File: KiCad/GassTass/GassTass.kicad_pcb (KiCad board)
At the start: 2 copper layers, 3 parts, among them U1 Arduino_Nano_v3.x, U2 ATmega328P-PU

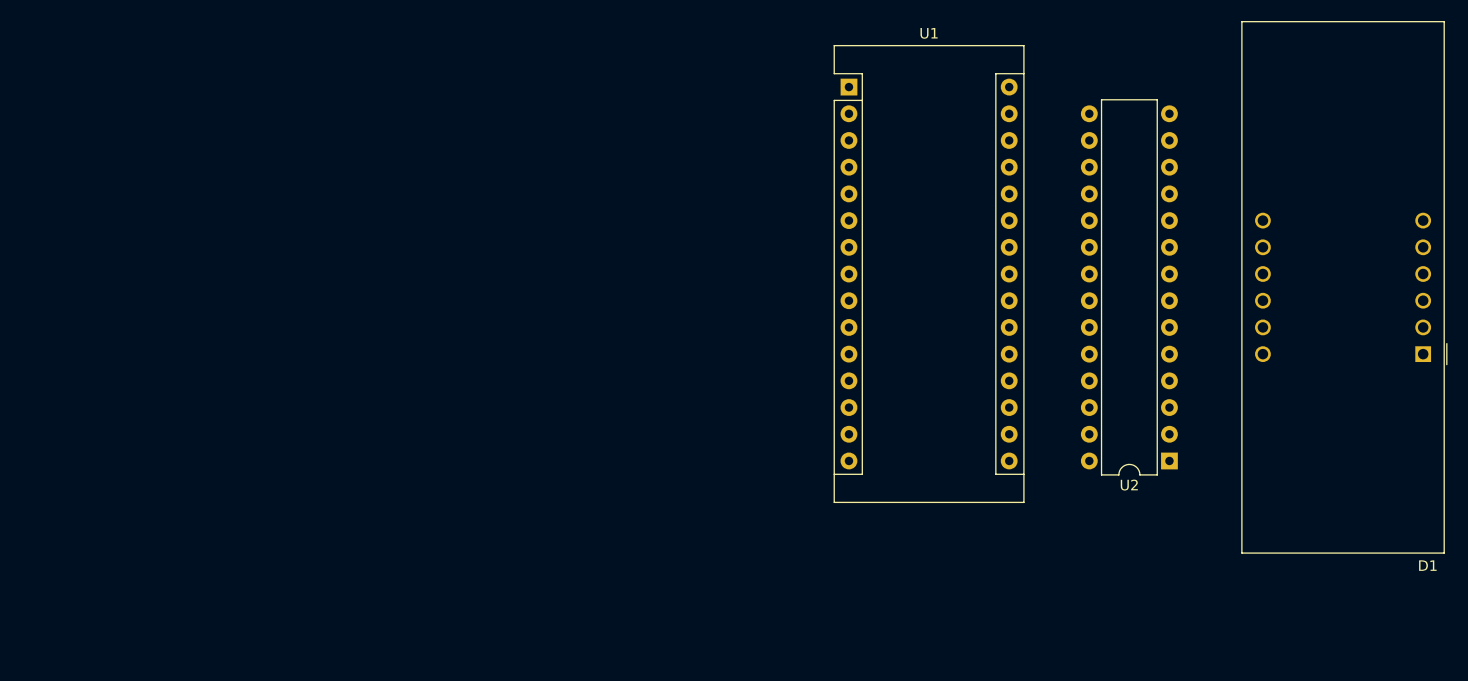
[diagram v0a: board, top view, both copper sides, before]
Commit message: at it again, adding transistors
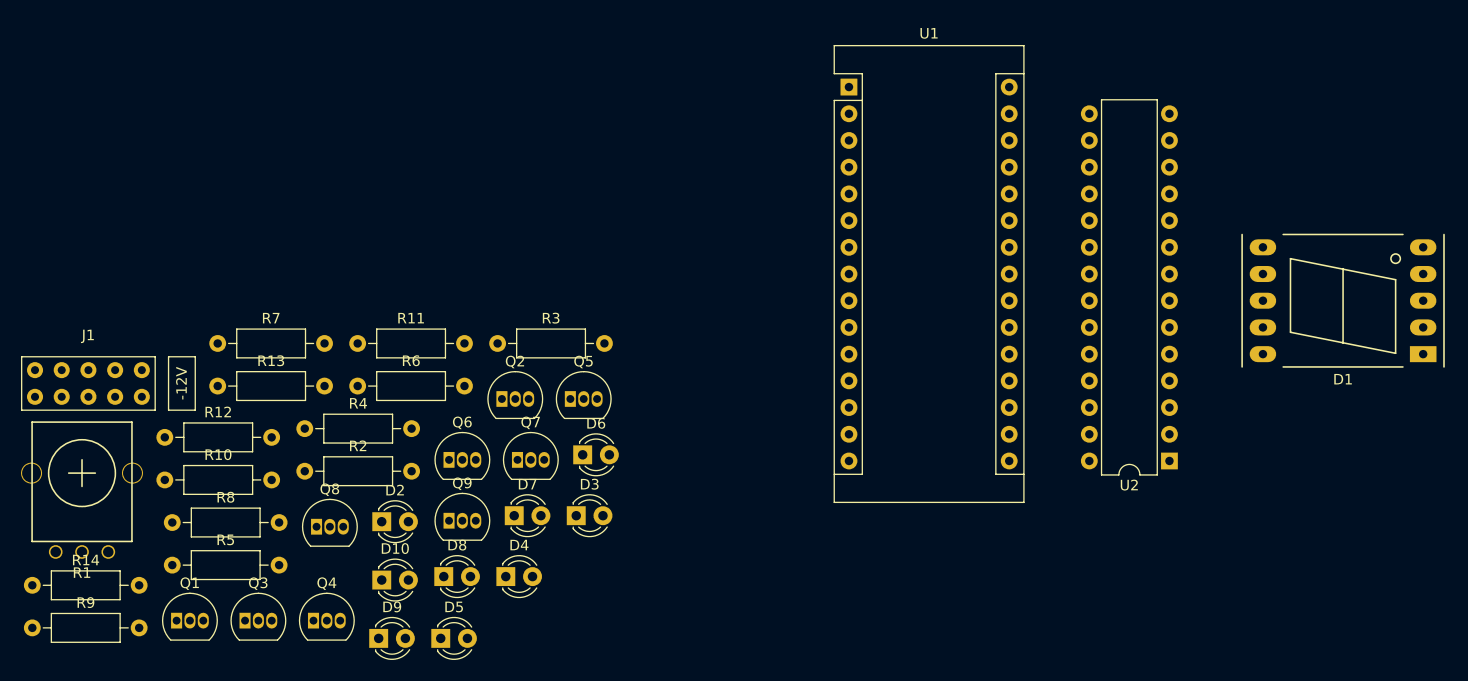
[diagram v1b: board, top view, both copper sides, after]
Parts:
- added D10: LED, LED_THT:LED_D3.0mm_FlatTop, F.Cu at (86.4, 99.0)
- added D2: LED, LED_THT:LED_D3.0mm_FlatTop, F.Cu at (86.4, 93.4)
- added D3: LED, LED_THT:LED_D3.0mm_FlatTop, F.Cu at (104.9, 92.8)
- added D4: LED, LED_THT:LED_D3.0mm_FlatTop, F.Cu at (98.2, 98.6)
- added D5: LED, LED_THT:LED_D3.0mm_FlatTop, F.Cu at (92.0, 104.5)
- added D6: LED, LED_THT:LED_D3.0mm_FlatTop, F.Cu at (105.5, 87.0)
- added D7: LED, LED_THT:LED_D3.0mm_FlatTop, F.Cu at (99.0, 92.8)
- added D8: LED, LED_THT:LED_D3.0mm_FlatTop, F.Cu at (92.3, 98.6)
- added D9: LED, LED_THT:LED_D3.0mm_FlatTop, F.Cu at (86.1, 104.5)
- added J1: EURO_PWR_2x5, eurorack:europwr2x5, F.Cu at (58.5, 75.2)
- added Q1: 2N3904, Package_TO_SOT_THT:TO-92_Inline, F.Cu at (66.9, 102.8)
- added Q2: 2N3904, Package_TO_SOT_THT:TO-92_Inline, F.Cu at (97.8, 81.7)
- added Q3: 2N3904, Package_TO_SOT_THT:TO-92_Inline, F.Cu at (73.4, 102.8)
- added Q4: 2N3904, Package_TO_SOT_THT:TO-92_Inline, F.Cu at (79.9, 102.8)
- added Q5: 2N3904, Package_TO_SOT_THT:TO-92_Inline, F.Cu at (104.3, 81.7)
- added Q6: 2N3904, Package_TO_SOT_THT:TO-92_Inline, F.Cu at (92.8, 87.5)
- added Q7: 2N3904, Package_TO_SOT_THT:TO-92_Inline, F.Cu at (99.3, 87.5)
- added Q8: 2N3904, Package_TO_SOT_THT:TO-92_Inline, F.Cu at (80.2, 93.9)
- added Q9: 2N3904, Package_TO_SOT_THT:TO-92_Inline, F.Cu at (92.8, 93.3)
- added R1: R_POT_US, eurorack:Alpha9mmPot, F.Cu at (57.9, 88.8)
- added R10: R_US, Resistor_THT:R_Axial_DIN0207_L6.3mm_D2.5mm_P10.16mm_Horizontal, F.Cu at (65.7, 89.4)
- added R11: R_US, Resistor_THT:R_Axial_DIN0207_L6.3mm_D2.5mm_P10.16mm_Horizontal, F.Cu at (84.1, 76.5)
- added R12: R_US, Resistor_THT:R_Axial_DIN0207_L6.3mm_D2.5mm_P10.16mm_Horizontal, F.Cu at (65.7, 85.4)
- added R13: R_US, Resistor_THT:R_Axial_DIN0207_L6.3mm_D2.5mm_P10.16mm_Horizontal, F.Cu at (70.8, 80.5)
- added R14: R_US, Resistor_THT:R_Axial_DIN0207_L6.3mm_D2.5mm_P10.16mm_Horizontal, F.Cu at (53.1, 99.5)
- added R2: R_US, Resistor_THT:R_Axial_DIN0207_L6.3mm_D2.5mm_P10.16mm_Horizontal, F.Cu at (79.1, 88.6)
- added R3: R_US, Resistor_THT:R_Axial_DIN0207_L6.3mm_D2.5mm_P10.16mm_Horizontal, F.Cu at (97.4, 76.5)
- added R4: R_US, Resistor_THT:R_Axial_DIN0207_L6.3mm_D2.5mm_P10.16mm_Horizontal, F.Cu at (79.1, 84.6)
- added R5: R_US, Resistor_THT:R_Axial_DIN0207_L6.3mm_D2.5mm_P10.16mm_Horizontal, F.Cu at (66.5, 97.5)
- added R6: R_US, Resistor_THT:R_Axial_DIN0207_L6.3mm_D2.5mm_P10.16mm_Horizontal, F.Cu at (84.1, 80.5)
- added R7: R_US, Resistor_THT:R_Axial_DIN0207_L6.3mm_D2.5mm_P10.16mm_Horizontal, F.Cu at (70.8, 76.5)
- added R8: R_US, Resistor_THT:R_Axial_DIN0207_L6.3mm_D2.5mm_P10.16mm_Horizontal, F.Cu at (66.5, 93.5)
- added R9: R_US, Resistor_THT:R_Axial_DIN0207_L6.3mm_D2.5mm_P10.16mm_Horizontal, F.Cu at (53.1, 103.5)
- D1: footprint Display_7Segment:CA56-12CGKWA -> Display_7Segment:7SegmentLED_LTS6760_LTS6780
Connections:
- U1 pad 29: Net-(R2-Pad1) -> GND
- U1 pad 4: Net-(R2-Pad1) -> GND
- U2 pad 22: Net-(R1-Pad1) -> GND
- U2 pad 8: Net-(R1-Pad1) -> GND
